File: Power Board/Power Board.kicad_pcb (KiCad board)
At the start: 4 copper layers, 194 parts, among them IC1 LTC4151IMS#PBF, J1 Conn_01x02, J10 Conn_01x02, J11 Conn_01x02, J12 Conn_01x02, J13 Conn_01x02, J14 Conn_01x02, J15 Conn_01x02, J16 Conn_01x02, J17 Conn_01x02, J18 Conn_02x03_Top_Bottom, J2 Conn_01x02, J20 Conn_02x03_Top_Bottom, J3 Conn_01x02, J4 Conn_01x02, J5 Conn_01x02, J6 Conn_01x02, J7 Conn_01x02, J8 Conn_01x02, J9 Conn_02x03_Top_Bottom, Q1 Q_PMOS_GDS, Q10 Q_NMOS_GDS, Q11 Q_NMOS_GDS, Q12 Q_NMOS_GDS, Q13 Q_NMOS_GDS, Q14 Q_NMOS_GDS, Q15 Q_NMOS_GDS, Q16 Q_NMOS_GDS, Q17 Q_NMOS_GDS, Q18 Q_NMOS_GDS, Q19 Q_NMOS_GDS, Q2 Q_PMOS_GDS, Q20 Q_NMOS_GDS, Q21 Q_NMOS_GDS, Q22 Q_NMOS_GDS, Q3 Q_PMOS_GDS, Q4 Q_PMOS_GDS, Q5 Q_PMOS_GDS, Q6 Q_PMOS_GDS, Q7 Q_PMOS_GDS, Q8 Q_PMOS_GDS, Q9 Q_NMOS_GDS, U1 LTC4372CDD-PBF, U10 ACS770xCB-050U-PFF, U11 ACS770xCB-050U-PFF, U12 ACS770xCB-050U-PFF, U13 ACS770xCB-050U-PFF, U14 ACS770xCB-050U-PFF, U15 ADC128S052CIMT, U16 ADC128S052CIMT, U17 TLV70033_SOT23-5, U2 LTC4372CDD-PBF, U3 LTC4372CDD-PBF, U4 LTC4372CDD-PBF, U5 LTC4372CDD-PBF, U6 LTC4372CDD-PBF, U7 LTC4372CDD-PBF, U8 ACS770xCB-050U-PFF, U9 ACS770xCB-050U-PFF

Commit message: more layout, power planes for 24V and 5V rails, current sensing and switch connections; might move digital section with ADCs and LTC4151s to bottom left
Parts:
- added IC2: LTC4151IMS#PBF, Package_SO:MSOP-10_3x3mm_P0.5mm, F.Cu at (219.3, 208.3)
- added RI2: 0.04, Resistor_SMD:R_0805_2012Metric_Pad1.20x1.40mm_HandSolder, F.Cu at (219.3, 212.9)
- IC1: footprint LTC4151:MSOP-10_MS_LIT -> Package_SO:MSOP-10_3x3mm_P0.5mm
- moved IC1 110.0 mm to (219.3, 261.8)
- moved RI1 109.5 mm to (219.1, 257.3)
- moved J_ROCKET1 90.3 mm to (107.1, 258.9), turned to 0 degrees
- moved C26 47.6 mm to (213.2, 242.3)
- moved C28 47.6 mm to (214.7, 246.0)
- moved C30 47.6 mm to (225.3, 246.8)
- moved C53 47.6 mm to (228.4, 242.5)
- moved R37 47.6 mm to (224.3, 234.1)
- moved RA10 47.6 mm to (212.3, 244.0)
- moved J20 47.6 mm to (237.5, 238.2)
- moved RA15 47.6 mm to (225.9, 242.5)
- moved U16 47.6 mm to (219.7, 239.6)
- moved C25 47.6 mm to (213.2, 236.9)
- moved C27 47.6 mm to (211.3, 242.3)
- moved C31 47.6 mm to (226.2, 246.8)
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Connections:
- IC1 pad 1: /24V_PSO -> /24V_PRESENSE
- IC1 pad 10: /24V_UNREGULATED -> /24V_REGULATED
- IC1 pad 2: /24V_PSO -> /24V_PRESENSE
- IC1 pad 3: /24V_PSO -> unconnected-(IC1-ADR1-Pad3)
- IC1 pad 6: /24V_MONITOR_SCL -> /SCL
- IC1 pad 7: /24V_MONITOR_SDA -> /SDA
- PS1 pad 4: /24V_REGULATED -> /24V_PRESENSE
- PS2 pad 6: /5V_REGULATED -> /5V_PSO
- RI1 pad 1: /24V_PSO -> /24V_PRESENSE
- RI1 pad 2: /24V_UNREGULATED -> /24V_REGULATED
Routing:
- net /SHDN: track 13.5 -> 186.2 mm
- net /24V_UNREGULATED: track 48.2 -> 120.9 mm
- net /3.3V: track 4.55 -> 54.2 mm, vias 2 -> 3
- net /24V_PRESENSE: track 0.00 -> 8.26 mm, vias 0 -> 1
- net /24V_REGULATED: track 0.00 -> 6.17 mm, vias 0 -> 1
- net /5V_REGULATED: track 88.7 -> 91.4 mm, vias 2 -> 4
- net Net-(D8-A): track 7.22 -> 4.92 mm
- net /ADC_1_DIN: track 11.1 -> 12.7 mm
- net /5V_PSO: vias 0 -> 2
- added copper zone on B.Cu, net /24V_PRESENSE
- added copper zone on F.Cu, net /24V_PSO
- added copper zone on B.Cu, net /24V_REGULATED
- added copper zone on F.Cu, net /24V_UNREGULATED
- added copper zone on B.Cu, net /5V_PSO
- added copper zone on B.Cu, net Net-(J8-Pin_2)
- added copper zone on F.Cu, net Net-(J8-Pin_2)
- added copper zone on B.Cu, net Net-(Q5-D)
- added copper zone on F.Cu, net Net-(Q5-D)
- added copper zone on B.Cu, net Net-(Q6-D)
- added copper zone on F.Cu, net Net-(Q6-D)
- added copper zone on B.Cu, net Net-(Q7-D)
- added copper zone on F.Cu, net Net-(Q7-D)
- added copper zone on B.Cu, net Net-(Q8-D)
- added copper zone on F.Cu, net Net-(Q8-D)

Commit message: aaryan jagtap
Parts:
- removed C25, C26, C27, C28, C29, C30, C31, C53: 22 nF, Capacitor_SMD:C_0201_0603Metric_Pad0.64x0.40mm_HandSolder
- removed C32, C33: 0.1 uF, Capacitor_SMD:C_0201_0603Metric_Pad0.64x0.40mm_HandSolder
- removed C34: 1 uF, Capacitor_SMD:C_0201_0603Metric_Pad0.64x0.40mm_HandSolder
- removed J10, J11, J12, J13, J14, J15, J16, J17: Conn_01x02, Connector_Molex:Molex_KK-254_AE-6410-02A_1x02_P2.54mm_Vertical
- removed J20: Conn_02x03_Top_Bottom, Connector_Molex:Molex_Nano-Fit_105314-xx06_2x03_P2.50mm_Horizontal
- removed R34, R35, R36, R37: 33, Resistor_SMD:R_0805_2012Metric_Pad1.20x1.40mm_HandSolder
- removed RA10, RA11, RA12, RA13, RA14, RA15, RA8, RA9: 100, Resistor_SMD:R_0805_2012Metric_Pad1.20x1.40mm_HandSolder
- removed RT1, RT2, RT3, RT4, RT5, RT6, RT7, RT8: 2.7K, Resistor_SMD:R_0805_2012Metric_Pad1.20x1.40mm_HandSolder
- removed U16: ADC128S052CIMT, ADC128S052CIMT_NOPB:SOP65P640X120-16N
- moved Q7 22.8 mm to (106.4, 163.7)
- moved R28 22.8 mm to (113.4, 162.8)
- moved R29 22.8 mm to (126.4, 163.0)
- moved U7 22.8 mm to (120.8, 163.2)
- moved C13 22.8 mm to (115.8, 163.4)
- moved C14 22.8 mm to (123.8, 164.0)
- moved D7 22.8 mm to (109.2, 170.2)
- moved Q21 22.8 mm to (124.2, 173.7)
- moved Q22 22.8 mm to (115.7, 173.7)
- moved R27 22.8 mm to (112.4, 166.8)
- moved R7 22.8 mm to (111.6, 170.8)
- moved C47 22.2 mm to (157.6, 168.6)
- moved C48 22.2 mm to (159.0, 168.6)
- moved C16 21.8 mm to (213.2, 203.8)
- moved C17 21.8 mm to (211.3, 203.8)
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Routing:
- net /5V_REGULATED: track 91.4 -> 17.6 mm
- net GND: track 63.8 -> 46.5 mm, vias 43 -> 32
- net Net-(J20-Pin_4): track 16.4 -> 0.00 mm, vias 1 -> 0
- net /ADC_2_DIN: track 11.1 -> 0.00 mm, vias 1 -> 0
- net Net-(J20-Pin_6): track 10.3 -> 0.00 mm, vias 1 -> 0
- net Net-(U16-IN7): track 9.80 -> 0.00 mm
- net /THERM_8: track 9.19 -> 0.00 mm, vias 1 -> 0
- net /THERM_1: track 8.65 -> 0.00 mm, vias 1 -> 0
- net Net-(U16-IN2): track 8.55 -> 0.00 mm
- net Net-(U16-IN3): track 8.47 -> 0.00 mm
- net /THERM_7: track 8.23 -> 0.00 mm, vias 1 -> 0
- net /ADC_2_CS: track 8.10 -> 0.00 mm, vias 2 -> 0
- net Net-(U16-IN4): track 7.88 -> 0.00 mm
- net /ADC_2_SCLK: track 7.72 -> 0.00 mm, vias 2 -> 0
- net Net-(U16-IN5): track 7.60 -> 0.00 mm
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
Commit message: removed thermistors and ADC; conserved space
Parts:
- moved IC1 0.71 mm to (218.8, 239.5)
- moved RI1 0.71 mm to (218.6, 235.0)
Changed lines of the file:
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@@
 	(footprint "Resistor_SMD:R_0805_2012Metric_Pad1.20x1.40mm_HandSolder"
 		(layer "F.Cu")
-		(at 219.060744 235.5)
+		(at 218.560744 235)
 		(descr "Resistor SMD 0805 (2012 Metric), square (rectangular) end terminal, IPC-7351 nominal with elongated pad for handsoldering. (Body size source: IPC-SM-782 page 72, https://www.pcb-3d.com/wordpress/wp-content/uploads/ipc-sm-782a_amendment_1_and_2.pdf), generated with kicad-footprint-generator")
 		(tags "resistor handsolder")
@@
 	(footprint "Package_SO:MSOP-10_3x3mm_P0.5mm"
 		(layer "F.Cu")
-		(at 219.260744 240)
+		(at 218.760744 239.5)
 		(descr "MSOP, 10 Pin (https://www.jedec.org/system/files/docs/mo-187F.pdf variant BA), generated with kicad-footprint-generator ipc_gullwing_generator.py")
 		(tags "MSOP SO Texas_DGS0010A")
@@
 	)
 	(segment
-		(start 220.060744 235.5)
-		(end 220.060744 237.6875)
+		(start 219.560744 235)
+		(end 219.560744 237.1875)
 		(width 0.25)
 		(layer "F.Cu")
@@
 	)
 	(segment
-		(start 221.373244 239)
-		(end 223.5 239)
+		(start 220.873244 238.5)
+		(end 223 238.5)
 		(width 0.25)
 		(layer "F.Cu")
@@
 	)
 	(segment
-		(start 220.060744 237.6875)
-		(end 221.373244 239)
+		(start 219.560744 237.1875)
+		(end 220.873244 238.5)
 		(width 0.25)
 		(layer "F.Cu")
@@
 	)
 	(via
-		(at 223.5 239)
+		(at 223 238.5)
 		(size 0.8)
 		(drill 0.4)
@@
 	)
 	(segment
-		(start 218.060744 238.5875)
-		(end 217.148244 239.5)
+		(start 217.560744 238.0875)
+		(end 216.648244 239)
 		(width 0.25)
 		(layer "F.Cu")
@@
 	)
 	(segment
-		(start 218.060744 235.5)
-		(end 218.060744 238.5875)
+		(start 217.560744 235)
+		(end 217.560744 238.0875)
 		(width 0.25)
 		(layer "F.Cu")
@@
 	)
 	(segment
-		(start 218.060744 235.5)
-		(end 218.060744 238.0875)
+		(start 217.560744 235)
+		(end 217.560744 237.5875)
 		(width 0.25)
 		(layer "F.Cu")
@@
 	)
 	(segment
-		(start 218.060744 238.0875)
-		(end 217.148244 239)
+		(start 217.560744 237.5875)
+		(end 216.648244 238.5)
 		(width 0.25)
 		(layer "F.Cu")
@@
 	)
 	(via
-		(at 218.060744 235.5)
+		(at 217.560744 235)
 		(size 0.8)
 		(drill 0.4)

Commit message: updated layout and pours
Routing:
- net /SHDN: track 186.2 -> 165.6 mm
- net /5V_REGULATED: vias 4 -> 3
- net /BATT_IN_12_2: vias 0 -> 20
- net /BATT_IN_12_1: vias 24 -> 28
- added copper zone on B.Cu, net Net-(Q10-S)

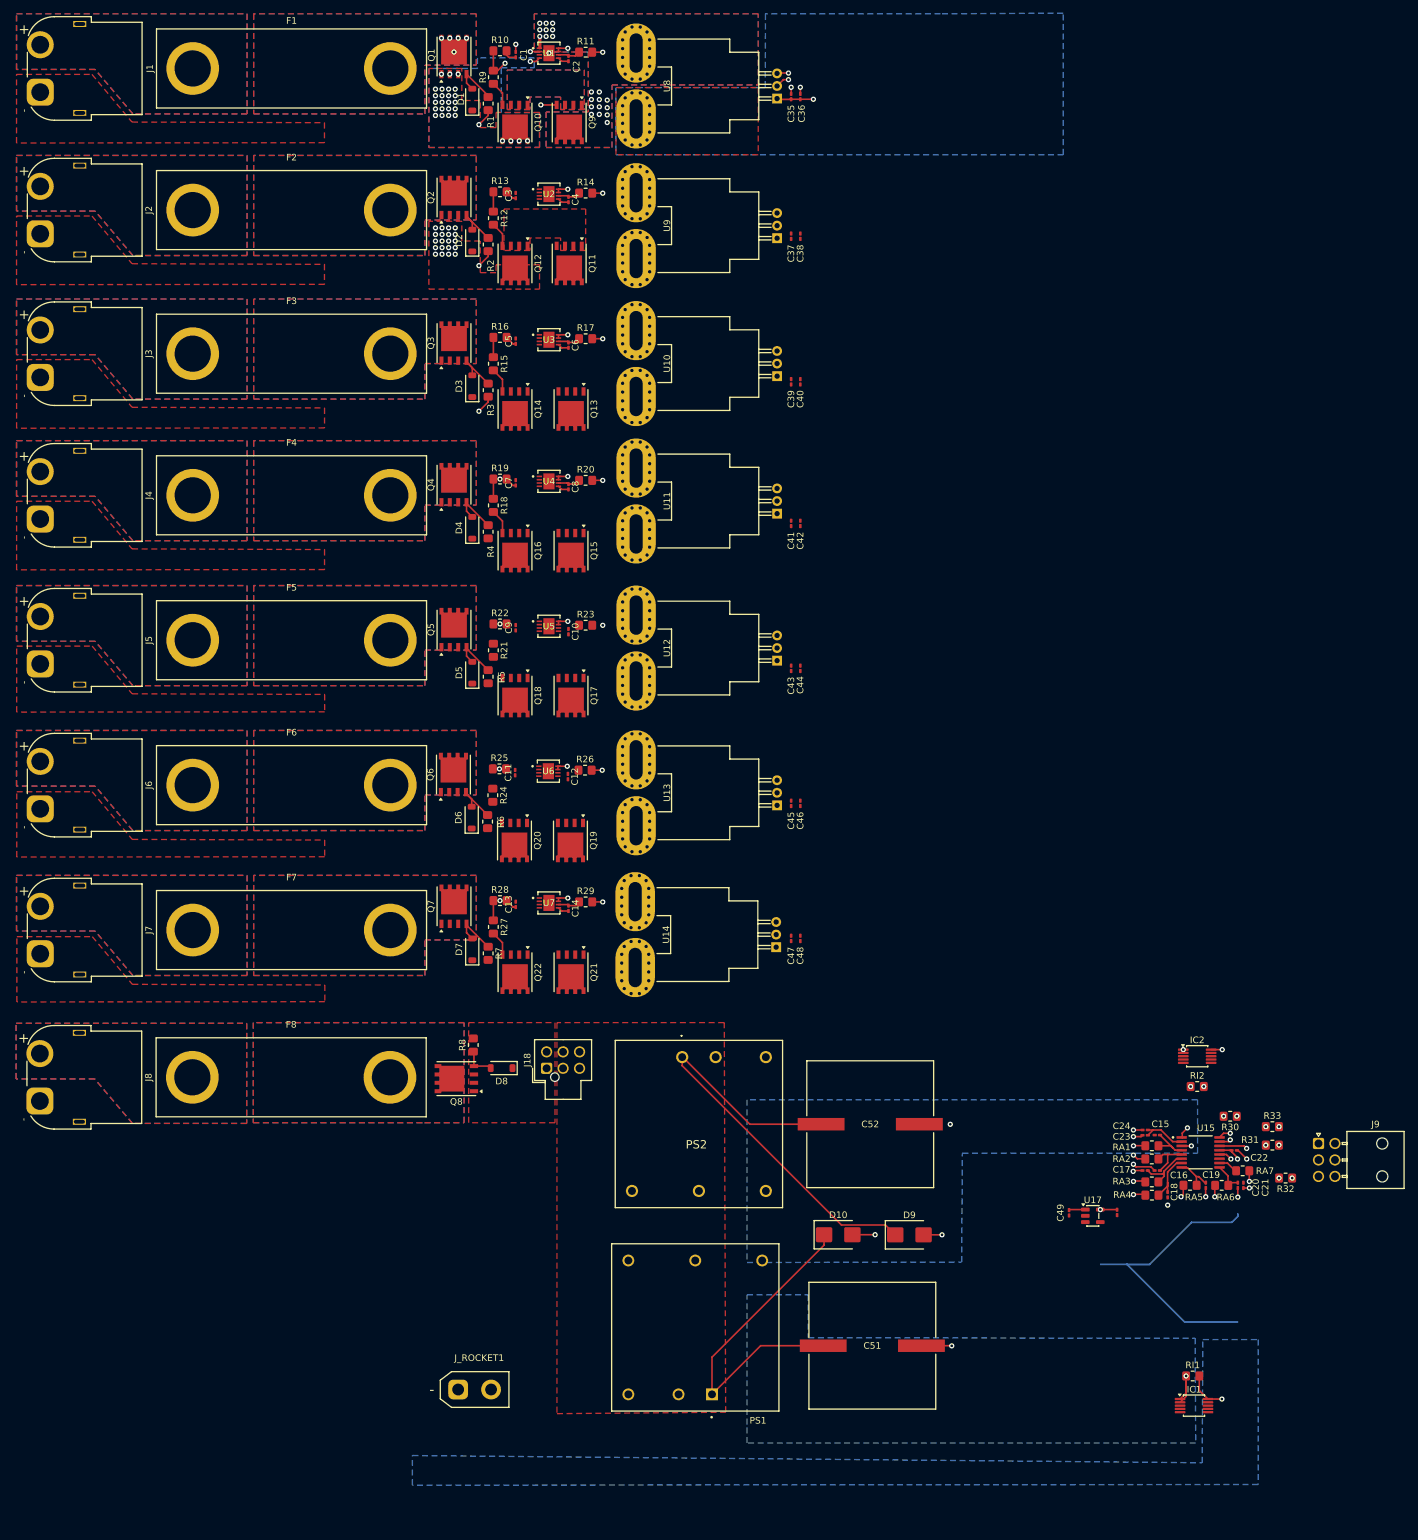
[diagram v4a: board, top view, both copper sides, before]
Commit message: updated xt60 connectors, routed ADC lines
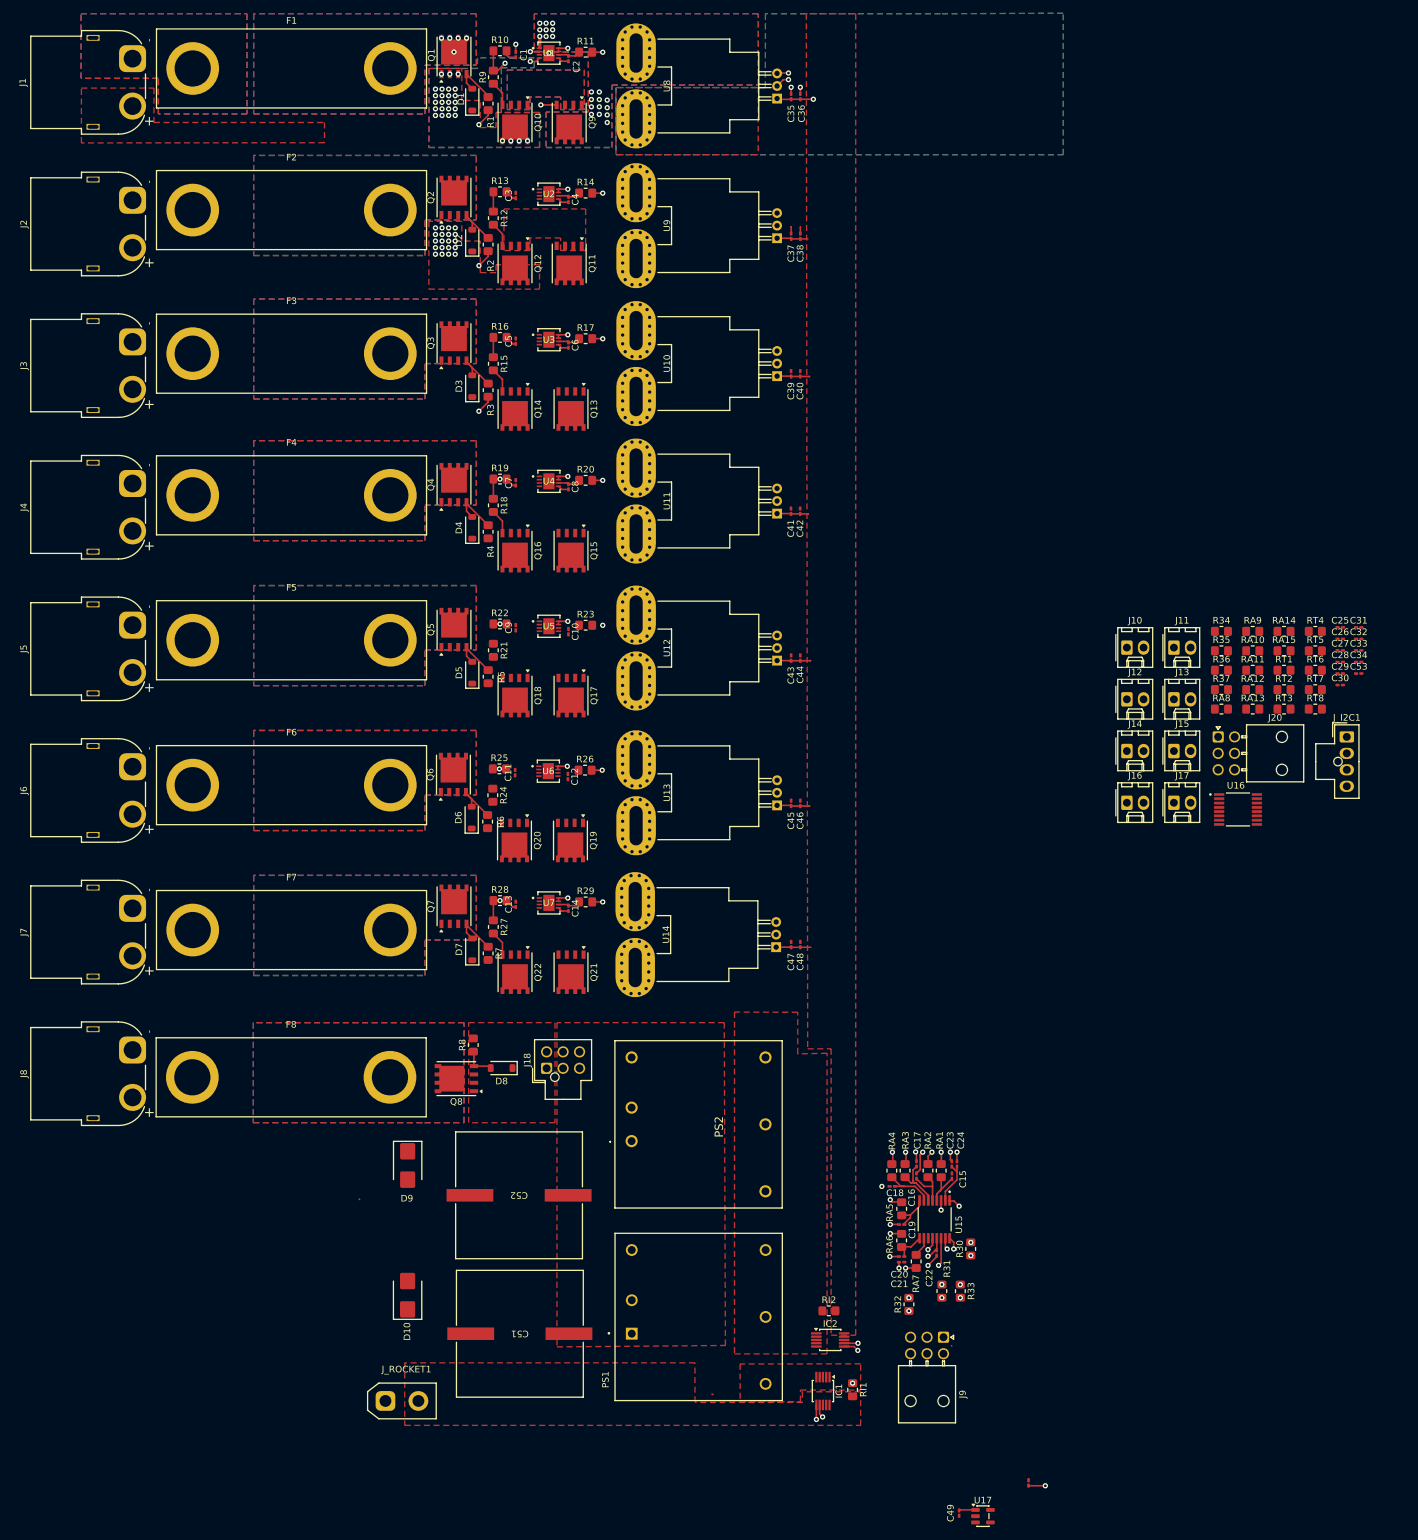
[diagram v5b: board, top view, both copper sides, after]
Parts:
- added C25: 22 nF, Capacitor_SMD:C_0201_0603Metric_Pad0.64x0.40mm_HandSolder, F.Cu at (241.0, 121.4)
- added C26: 22 nF, Capacitor_SMD:C_0201_0603Metric_Pad0.64x0.40mm_HandSolder, F.Cu at (241.0, 123.1)
- added C27: 22 nF, Capacitor_SMD:C_0201_0603Metric_Pad0.64x0.40mm_HandSolder, F.Cu at (241.0, 124.9)
- added C28: 22 nF, Capacitor_SMD:C_0201_0603Metric_Pad0.64x0.40mm_HandSolder, F.Cu at (241.0, 126.6)
- added C29: 22 nF, Capacitor_SMD:C_0201_0603Metric_Pad0.64x0.40mm_HandSolder, F.Cu at (241.0, 128.4)
- added C30: 22 nF, Capacitor_SMD:C_0201_0603Metric_Pad0.64x0.40mm_HandSolder, F.Cu at (241.0, 130.1)
- added C31: 22 nF, Capacitor_SMD:C_0201_0603Metric_Pad0.64x0.40mm_HandSolder, F.Cu at (243.8, 121.4)
- added C32: 0.1 uF, Capacitor_SMD:C_0201_0603Metric_Pad0.64x0.40mm_HandSolder, F.Cu at (243.8, 123.1)
- added C33: 0.1 uF, Capacitor_SMD:C_0201_0603Metric_Pad0.64x0.40mm_HandSolder, F.Cu at (243.8, 124.9)
- added C34: 1 uF, Capacitor_SMD:C_0201_0603Metric_Pad0.64x0.40mm_HandSolder, F.Cu at (243.8, 126.6)
- added C53: 22 nF, Capacitor_SMD:C_0201_0603Metric_Pad0.64x0.40mm_HandSolder, F.Cu at (243.8, 128.4)
- added J10: Conn_01x02, Connector_Molex:Molex_KK-254_AE-6410-02A_1x02_P2.54mm_Vertical, F.Cu at (208.6, 124.4)
- added J11: Conn_01x02, Connector_Molex:Molex_KK-254_AE-6410-02A_1x02_P2.54mm_Vertical, F.Cu at (215.7, 124.4)
- added J12: Conn_01x02, Connector_Molex:Molex_KK-254_AE-6410-02A_1x02_P2.54mm_Vertical, F.Cu at (208.6, 132.3)
- added J13: Conn_01x02, Connector_Molex:Molex_KK-254_AE-6410-02A_1x02_P2.54mm_Vertical, F.Cu at (215.7, 132.3)
- added J14: Conn_01x02, Connector_Molex:Molex_KK-254_AE-6410-02A_1x02_P2.54mm_Vertical, F.Cu at (208.6, 140.1)
- added J15: Conn_01x02, Connector_Molex:Molex_KK-254_AE-6410-02A_1x02_P2.54mm_Vertical, F.Cu at (215.7, 140.1)
- added J16: Conn_01x02, Connector_Molex:Molex_KK-254_AE-6410-02A_1x02_P2.54mm_Vertical, F.Cu at (208.6, 148.0)
- added J17: Conn_01x02, Connector_Molex:Molex_KK-254_AE-6410-02A_1x02_P2.54mm_Vertical, F.Cu at (215.7, 148.0)
- added J20: Conn_02x03_Top_Bottom, Connector_Molex:Molex_Nano-Fit_105314-xx06_2x03_P2.50mm_Horizontal, F.Cu at (222.4, 138.0)
- added J_I2C1: Conn_02x02_Counter_Clockwise, Connector_Molex:Molex_Nano-Fit_105309-xx04_1x04_P2.50mm_Vertical, F.Cu at (242.0, 138.0)
- added R34: 33, Resistor_SMD:R_0805_2012Metric_Pad1.20x1.40mm_HandSolder, F.Cu at (222.9, 122.0)
- added R35: 33, Resistor_SMD:R_0805_2012Metric_Pad1.20x1.40mm_HandSolder, F.Cu at (222.9, 124.9)
- added R36: 33, Resistor_SMD:R_0805_2012Metric_Pad1.20x1.40mm_HandSolder, F.Cu at (222.9, 127.9)
- added R37: 33, Resistor_SMD:R_0805_2012Metric_Pad1.20x1.40mm_HandSolder, F.Cu at (222.9, 130.8)
- added RA10: 100, Resistor_SMD:R_0805_2012Metric_Pad1.20x1.40mm_HandSolder, F.Cu at (227.7, 124.9)
- added RA11: 100, Resistor_SMD:R_0805_2012Metric_Pad1.20x1.40mm_HandSolder, F.Cu at (227.7, 127.9)
- added RA12: 100, Resistor_SMD:R_0805_2012Metric_Pad1.20x1.40mm_HandSolder, F.Cu at (227.7, 130.8)
- added RA13: 100, Resistor_SMD:R_0805_2012Metric_Pad1.20x1.40mm_HandSolder, F.Cu at (227.7, 133.8)
- added RA14: 100, Resistor_SMD:R_0805_2012Metric_Pad1.20x1.40mm_HandSolder, F.Cu at (232.4, 122.0)
- added RA15: 100, Resistor_SMD:R_0805_2012Metric_Pad1.20x1.40mm_HandSolder, F.Cu at (232.4, 124.9)
- added RA8: 100, Resistor_SMD:R_0805_2012Metric_Pad1.20x1.40mm_HandSolder, F.Cu at (222.9, 133.8)
- added RA9: 100, Resistor_SMD:R_0805_2012Metric_Pad1.20x1.40mm_HandSolder, F.Cu at (227.7, 122.0)
- added RT1: 2.7K, Resistor_SMD:R_0805_2012Metric_Pad1.20x1.40mm_HandSolder, F.Cu at (232.4, 127.9)
- added RT2: 2.7K, Resistor_SMD:R_0805_2012Metric_Pad1.20x1.40mm_HandSolder, F.Cu at (232.4, 130.8)
- added RT3: 2.7K, Resistor_SMD:R_0805_2012Metric_Pad1.20x1.40mm_HandSolder, F.Cu at (232.4, 133.8)
- added RT4: 2.7K, Resistor_SMD:R_0805_2012Metric_Pad1.20x1.40mm_HandSolder, F.Cu at (237.2, 122.0)
- added RT5: 2.7K, Resistor_SMD:R_0805_2012Metric_Pad1.20x1.40mm_HandSolder, F.Cu at (237.2, 124.9)
- added RT6: 2.7K, Resistor_SMD:R_0805_2012Metric_Pad1.20x1.40mm_HandSolder, F.Cu at (237.2, 127.9)
- added RT7: 2.7K, Resistor_SMD:R_0805_2012Metric_Pad1.20x1.40mm_HandSolder, F.Cu at (237.2, 130.8)
- added RT8: 2.7K, Resistor_SMD:R_0805_2012Metric_Pad1.20x1.40mm_HandSolder, F.Cu at (237.2, 133.8)
- added U16: ADC128S052CIMT, ADC128S052CIMT_NOPB:SOP65P640X120-16N, F.Cu at (225.4, 149.0)
- moved D9 76.9 mm to (99.4, 203.0), turned to -90 degrees
- moved IC2 70.4 mm to (163.5, 229.5)
- moved D10 66.0 mm to (99.4, 222.7), turned to 90 degrees
- moved RI2 65.5 mm to (163.3, 225.1)
- moved J9 64.1 mm to (180.7, 229.1), turned to -90 degrees
- moved R32 60.3 mm to (175.5, 224.1), turned to 90 degrees
- moved IC1 56.4 mm to (162.4, 237.3), turned to -90 degrees
- moved R31 54.9 mm to (180.5, 222.1), turned to 90 degrees
- moved C52 54.4 mm to (116.3, 207.6), turned to 180 degrees
- moved R33 53.5 mm to (183.3, 222.1), turned to -90 degrees
- moved C51 53.5 mm to (116.4, 228.6), turned to 0 degrees
- moved C21 53.2 mm to (174.4, 217.7), turned to 180 degrees
- moved C20 52.2 mm to (174.4, 216.9), turned to 180 degrees
- moved RI1 51.7 mm to (166.9, 237.1), turned to -90 degrees
- moved RA7 51.4 mm to (176.6, 217.6), turned to 90 degrees
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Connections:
- F1 pad 1: Net-(J1-Pin_2) -> Net-(J1-Pin_1)
- F2 pad 1: Net-(J2-Pin_2) -> Net-(J2-Pin_1)
- F3 pad 1: Net-(J3-Pin_2) -> Net-(J3-Pin_1)
- F4 pad 1: Net-(J4-Pin_2) -> Net-(J4-Pin_1)
- F5 pad 1: Net-(J5-Pin_2) -> Net-(J5-Pin_1)
- F6 pad 1: Net-(J6-Pin_2) -> Net-(J6-Pin_1)
- F8 pad 1: Net-(J8-Pin_2) -> Net-(J8-Pin_1)
- J1 pad 1: GND -> Net-(J1-Pin_1)
- J1 pad 2: Net-(J1-Pin_2) -> GND
- J2 pad 1: GND -> Net-(J2-Pin_1)
- J2 pad 2: Net-(J2-Pin_2) -> GND
- J3 pad 1: GND -> Net-(J3-Pin_1)
- J3 pad 2: Net-(J3-Pin_2) -> GND
- J4 pad 1: GND -> Net-(J4-Pin_1)
- J4 pad 2: Net-(J4-Pin_2) -> GND
- J5 pad 1: GND -> Net-(J5-Pin_1)
- J5 pad 2: Net-(J5-Pin_2) -> GND
- J6 pad 1: GND -> Net-(J6-Pin_1)
- J6 pad 2: Net-(J6-Pin_2) -> GND
- J8 pad 1: GND -> Net-(J8-Pin_1)
- J8 pad 2: Net-(J8-Pin_2) -> GND
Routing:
- net /BATT_1_SENSE: track 3.46 -> 177.6 mm
- net /BATT_2_SENSE: track 1.98 -> 155.4 mm
- net /BATT_3_SENSE: track 1.65 -> 132.9 mm
- net /24V_UNREGULATED: track 120.9 -> 0.15 mm
- net /BATT_4_SENSE: track 1.79 -> 109.9 mm
- net /BATT_5_SENSE: track 1.84 -> 94.6 mm
- net /BATT_6_SENSE: track 1.63 -> 78.6 mm
- net /BATT_7_SENSE: track 1.94 -> 62.6 mm
- net /3.3V: track 50.9 -> 6.25 mm
- net /5V_REGULATED: track 17.6 -> 46.1 mm, vias 3 -> 1
- net GND: track 46.5 -> 38.2 mm, vias 32 -> 28
- net /24V_PRESENSE: track 8.26 -> 0.00 mm
- net /24V_REGULATED: track 6.17 -> 0.00 mm, vias 1 -> 0
- net /SCL: track 0.00 -> 4.52 mm, vias 0 -> 2
- net /SDA: track 0.00 -> 4.11 mm, vias 0 -> 2
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- added copper zone on F.Cu, net /24V_PRESENSE
- added copper zone on F.Cu, net /24V_REGULATED
- added copper zone on F.Cu, net /5V_PSO
- added copper zone on F.Cu, net /5V_REGULATED
- added copper zone on B.Cu, net GND
- removed copper zone on B.Cu, net /24V_PRESENSE
- removed copper zone on B.Cu, net /24V_REGULATED
- removed copper zone on B.Cu, net /5V_PSO
- removed copper zone on In2.Cu, net /5V_REGULATED
- removed copper zone on B.Cu, net Net-(J1-Pin_2)
- removed copper zone on F.Cu, net Net-(J1-Pin_2)
- removed copper zone on B.Cu, net Net-(J2-Pin_2)
- removed copper zone on F.Cu, net Net-(J2-Pin_2)
- removed copper zone on B.Cu, net Net-(J3-Pin_2)
- removed copper zone on F.Cu, net Net-(J3-Pin_2)
- removed copper zone on B.Cu, net Net-(J4-Pin_2)
- removed copper zone on F.Cu, net Net-(J4-Pin_2)
- removed copper zone on B.Cu, net Net-(J5-Pin_2)
- removed copper zone on F.Cu, net Net-(J5-Pin_2)
- removed copper zone on B.Cu, net Net-(J6-Pin_2)
- removed copper zone on F.Cu, net Net-(J6-Pin_2)
- removed copper zone on B.Cu, net Net-(J7-Pin_2)
- removed copper zone on F.Cu, net Net-(J7-Pin_2)
- removed copper zone on B.Cu, net Net-(J8-Pin_2)
- removed copper zone on F.Cu, net Net-(J8-Pin_2)
